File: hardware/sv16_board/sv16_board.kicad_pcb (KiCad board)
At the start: 4 copper layers, 100 x 100 mm, 141 parts, among them J1 JTAG, J10 CONSOLE, J2 JTAG-1.27, J3 EXP-A, J4 EXP-B, J5 EXP-C, J6 MOTOR, J7 SPARE (not fitted), J8 USB-C, J9 7-12 V, Q1 2N7002, Q2 BC817, Q4 BC807, SW1 RESET, SW2 RECONFIG, U1 LFE5U-12F-6TG144C, U2 W25Q64JVSSIQ, U3 W25Q64JVSSIQ, U4 CH340G, U5 AP62300TWU-7, U6 MP1584EN, U7 LP5907MFX-2.5, U8 USBLC6-2SC6, Y1 25 MHz ACTIVE XO (4-pin), Y2 12 MHz (CH340G clock)

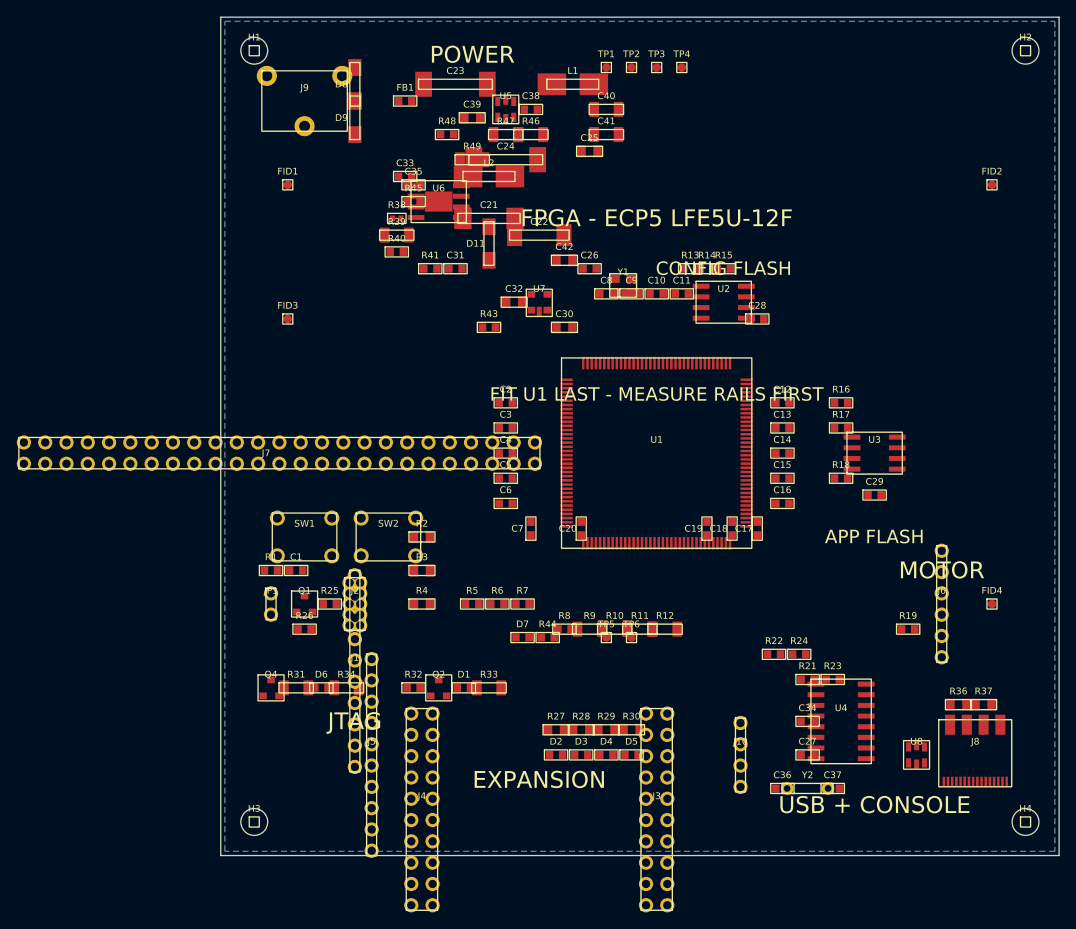
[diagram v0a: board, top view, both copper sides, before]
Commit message: The board, generated and checked: connections, copper, bitmaps, BOM/CPL
Everything a person needs to take the SV-16 PCB from "footprints and a netlist"
to a routed, orderable board, generated from one source of truth so no picture,
no BOM line and no connection can disagree with the board file.

PCB_CONNECTIONS.md (and .pdf) - the file that was asked for: the connections
written and drawn.  Every pad of every part with its net and the other pads on
that net, in build order; every connector pinout; the power tree with the real
numbers; the FPGA pin table straight from the LPF; what the copper generator
already connected and the seven pads the router still owes a trace; the twelve
checks before routing; the six connection sheets drawn.  Generated by
scripts/sv16_pcb_connections.py and checked for staleness by `make lint`.

scripts/sv16_pcb_copper.py - the copper that can be worked out without a human
at the mouse, now in the board file:
  * rail pours on In2.Cu (3V3 whole-layer, 1V1 and 2V5 patches with priorities)
  * 291 vias: an escape via with a 0.2 mm stub on every surface-mount pad that
    sits over its own rail's pour (GND 217, 3V3 55, 1V1 11, 2V5 8), the MP1584's
    exposed pad thermally stitched, 128 GND stitching vias in two edge rings
  * every via checked against every other pad for clearance before it is written;
    pads that sit over the wrong rail are reported, not shorted

scripts/sv16_pcb_bitmap.py - five bitmaps: top and bottom views of the board
(pads, silkscreen, pours, vias, DNP marks), the ratsnest by function, the power
tree and pour map, and the six connection sheets.  Drawn from the same data.

scripts/sv16_pcb_bom.py - BOM.csv (grouped, with part numbers and a DNP column),
JLCPCB_BOM.csv and JLCPCB_CPL.csv in the columns an assembly service wants, and
FAB_NOTES.md (stack-up, rules, gerber settings, what to upload).

Placement repair: the hand-typed floorplan table had ~50 pad pairs of different
nets within 0.2 mm - a short before the board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
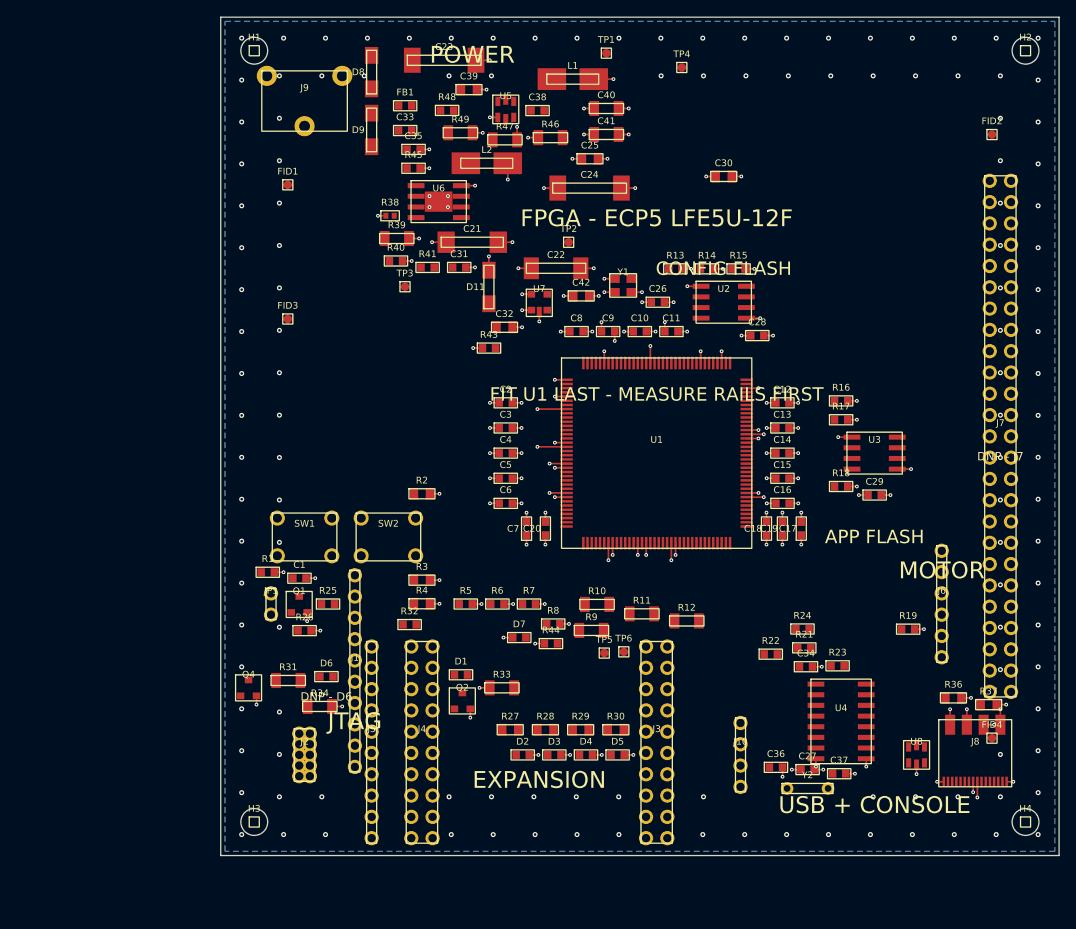
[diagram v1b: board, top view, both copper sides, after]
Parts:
- moved J7 86.0 mm to (93.0, 50.0), turned to 0 degrees
- moved TP3 39.8 mm to (22.0, 32.1)
- moved C30 26.2 mm to (60.0, 19.0)
- moved TP2 22.2 mm to (41.5, 26.9)
- moved J2 19.0 mm to (10.0, 88.0)
- moved FID4 16.0 mm to (92.0, 86.0)
- moved C24 10.6 mm to (44.0, 20.4)
- moved C26 9.07 mm to (52.1, 34.0)
- moved C19 9.00 mm to (67.0, 61.0)
- moved J3 8.00 mm to (52.0, 86.5)
- moved J4 8.00 mm to (24.0, 86.5)
- moved R32 7.56 mm to (22.5, 72.5)
- moved C34 6.52 mm to (69.8, 77.5)
- moved FID2 6.00 mm to (92.0, 14.0)
- moved C8 5.74 mm to (42.4, 37.5)
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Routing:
- net GND: track 0.00 -> 112.9 mm, vias 0 -> 217
- net 3V3: track 0.00 -> 68.4 mm, vias 0 -> 55
- net 1V1: track 0.00 -> 18.1 mm, vias 0 -> 11
- net 2V5: track 0.00 -> 10.2 mm, vias 0 -> 8
- added copper zone on In2.Cu, net 1V1
- added copper zone on In2.Cu, net 2V5
- added copper zone on In2.Cu, net 3V3
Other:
- board text added: "DNP - D6"
- board text added: "DNP - J7"

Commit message: schematic: the KiCad schematic, generated from the board netlist
The board's wiring has had two forms until now - the .kicad_pcb and
PCB_CONNECTIONS.md.  This adds the third, and the one KiCad users ask for
first: hardware/sv16_board/sv16_board.kicad_sch

  * 143 symbols, one per part, in the ten blocks of PCB_CONNECTIONS.md
  * 596 pins, 472 of them on a wire stub with the net name as a label
    ("same label = same net", so the whole board is wired by name)
  * 124 unused pins carry a no-connect cross
  * the FPGA's pin 133 is labelled `clk_25m`, straight from the LPF

It is generated by scripts/sv16_pcb_schematic.py from the same COMPONENTS /
CONNECTIONS tables that place the board's footprints, so the schematic and the
PCB cannot drift.  `--check` re-parses the file and audits it against the
netlist *per net* - a label on the wrong pin keeps the total right, so totals
are not enough.

  make schematic                  # write it (+ schematic_preview.png)
  make pcb                        # now writes the schematic first
  make pcb-check / make lint      # now re-verify it

Also lands the pending PCB work: the copper plan/bitmap/BOM/connections
deliverable set, the board regenerated against the current plan (266 vias,
156 stubs), and the router's geometric self-check gates.

Co-authored-by: arena-agent <297053741+arena-agent@users.noreply.github.com>
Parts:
- moved R36 12.8 mm to (85.0, 93.8)
- moved R37 12.0 mm to (89.2, 93.8)
- moved FID4 7.77 mm to (92.5, 93.8)
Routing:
- net GND: track 112.9 -> 106.0 mm, vias 217 -> 195
- net 3V3: track 68.4 -> 62.3 mm, vias 55 -> 52
